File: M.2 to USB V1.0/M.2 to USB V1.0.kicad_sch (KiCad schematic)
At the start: 16 parts, among them IC1 USB2422T_MJ, IC2 TPS2041CDBVT, IC3 TPS2041CDBVT, J1 M.2 Slot, U1 APX809-46SRG-7

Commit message: updated schematic
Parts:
- added IC4: TPS61230ARNST, Component Library:RNS0007A, symbol TPS61230ARNST:TPS61230ARNST
- added R4: 100kΩ, Resistor_SMD:R_0402_1005Metric_Pad0.72x0.64mm_HandSolder, symbol Device:R_US
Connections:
- net GND: now also R4.2
- net at IC1.17 (SUSP_IND/LOCAL_PWR/(NON_REM0)): now also R4.1
- no-connect marks 58 -> 60
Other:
- moved on the sheet: C5, C6, C7, C8, IC1, R1

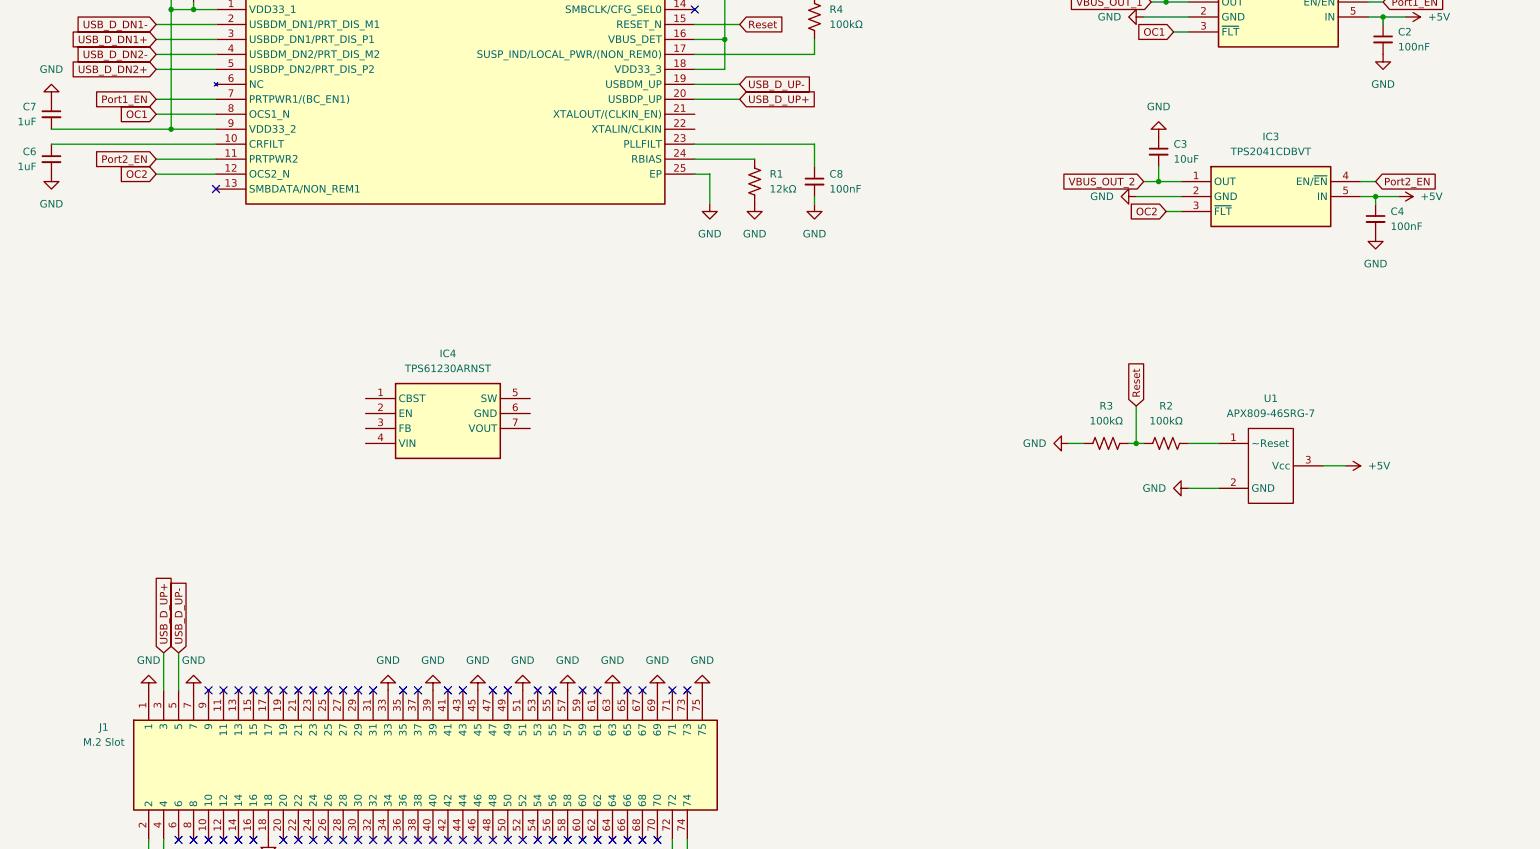
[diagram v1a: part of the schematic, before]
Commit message: finished schematic
finished schematic values of crystal caps not set. will be set after board design
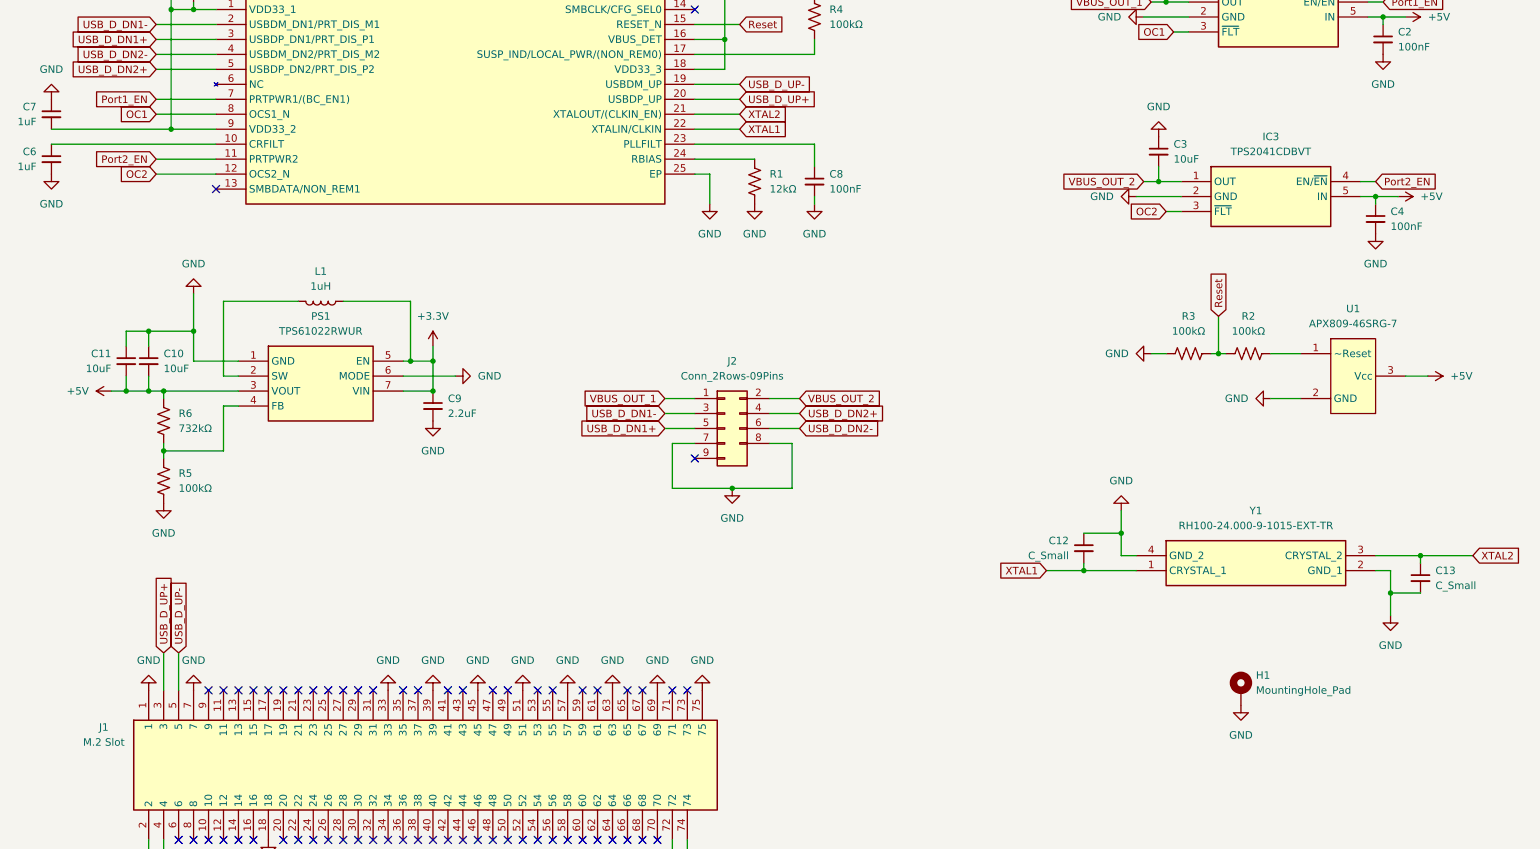
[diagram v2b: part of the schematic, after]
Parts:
- removed IC4: TPS61230ARNST, Component Library:RNS0007A, symbol TPS61230ARNST:TPS61230ARNST
- added C10, C11: 10uF, Capacitor_SMD:C_0402_1005Metric_Pad0.74x0.62mm_HandSolder, symbol Device:C_Small
- added C12, C13: C_Small, Capacitor_SMD:C_0402_1005Metric_Pad0.74x0.62mm_HandSolder, symbol Device:C_Small
- added C9: 2.2uF, Capacitor_SMD:C_0402_1005Metric_Pad0.74x0.62mm_HandSolder, symbol Device:C_Small
- added H1: MountingHole_Pad, Component Library:m.2 edge mount hole, symbol Mechanical:MountingHole_Pad
- added J2: Conn_2Rows-09Pins, symbol Connector_Generic:Conn_2Rows-09Pins
- added L1: 1uH, Inductor_SMD:L_Bourns_SRN6045TA, symbol Device:L
- added PS1: TPS61022RWUR, Component Library:TPS61022RWUR, symbol TPS61022RWUR:TPS61022RWUR
- added R5: 100kΩ, Resistor_SMD:R_0402_1005Metric_Pad0.72x0.64mm_HandSolder, symbol Device:R_US
- added R6: 732kΩ, Resistor_SMD:R_0402_1005Metric_Pad0.72x0.64mm_HandSolder, symbol Device:R_US
- added Y1: RH100-24.000-9-1015-EXT-TR, Component Library:RH10010000105050TR, symbol RH100-24_000-9-1015-EXT-TR:RH100-24.000-9-1015-EXT-TR
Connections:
- net +3.3V: now also C9.1, L1.1, PS1.5 (EN), PS1.7 (VIN)
- net +5V: now also C10.2, C11.2, PS1.3 (VOUT), R6.1
- net GND: now also C10.1, C11.1, C12.1, C13.2, C9.2, H1.1, J2.7 (Pin_7), J2.8 (Pin_8), PS1.1 (GND), PS1.6 (MODE), R5.2, Y1.2 (GND_1), Y1.4 (GND_2)
- net USB_D_DN1+: now also J2.5 (Pin_5)
- net USB_D_DN1-: now also J2.3 (Pin_3)
- net USB_D_DN2+: now also J2.4 (Pin_4)
- net USB_D_DN2-: now also J2.6 (Pin_6)
- net VBUS_OUT_1: now also J2.1 (Pin_1)
- net VBUS_OUT_2: now also J2.2 (Pin_2)
- net XTAL2: now reaches IC1.21 (XTALOUT/(CLKIN_EN))
- net XTAL2: now also C13.1, Y1.3 (CRYSTAL_2)
- net XTAL1: now reaches IC1.22 (XTALIN/CLKIN)
- net XTAL1: now also C12.2, Y1.1 (CRYSTAL_1)
- new net: PS1.4 (FB), R5.1, R6.2
- new net: L1.2, PS1.2 (SW)
- no-connect marks 60 -> 61
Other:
- moved on the sheet: R2, R3

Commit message: added all footprints
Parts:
- J2: footprint (none) -> Component Library:G821EU210AAL10Y
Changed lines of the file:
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@@
 			)
 		)
-		(property "Footprint" ""
+		(property "Footprint" "Component Library:G821EU210AAL10Y"
 			(at 137.16 107.95 0)
 			(effects

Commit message: finished pcb layout
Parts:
- J2: footprint Component Library:G821EU210AAL10Y -> Component Library:USB 2.0 Front Header
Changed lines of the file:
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@@
 			)
 		)
-		(property "Footprint" "Component Library:G821EU210AAL10Y"
+		(property "Footprint" "Component Library:USB 2.0 Front Header"
 			(at 137.16 107.95 0)
 			(effects

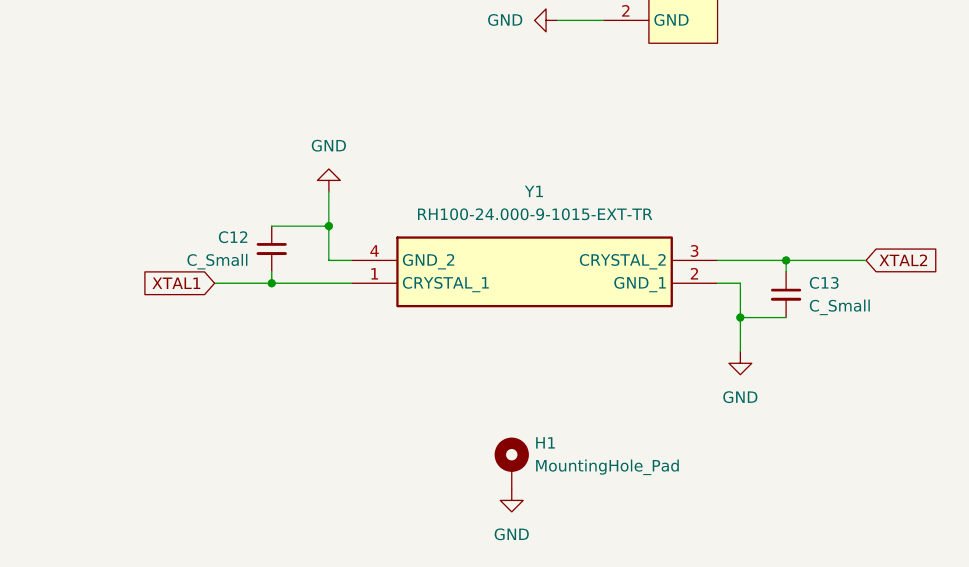
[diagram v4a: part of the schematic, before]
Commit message: updated pcb
updated pcb

calculated load caps

added 3D render
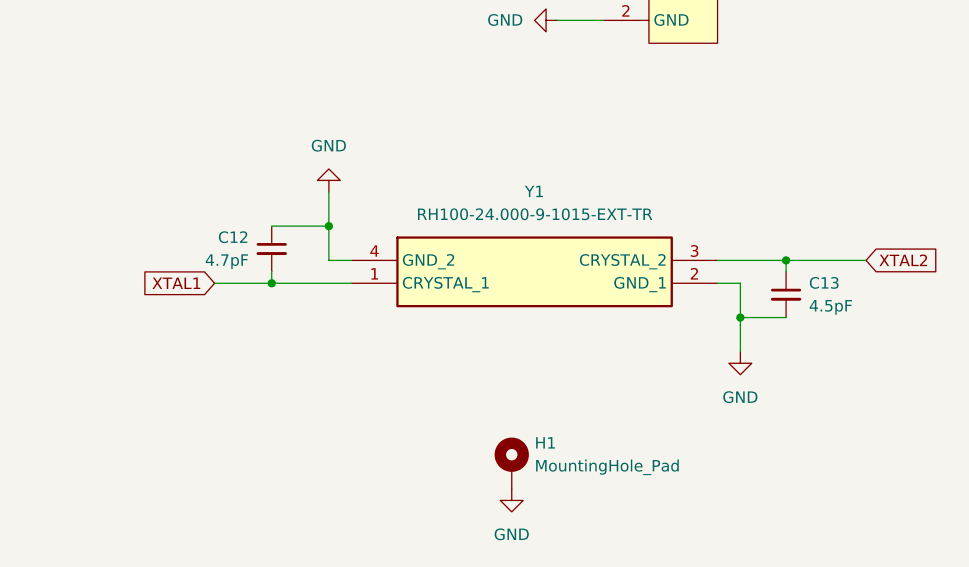
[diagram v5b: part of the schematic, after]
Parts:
- C12: value C_Small -> 4.7pF
- C13: value C_Small -> 4.5pF
- C5: footprint Capacitor_SMD:C_0402_1005Metric_Pad0.74x0.62mm_HandSolder -> Capacitor_SMD:C_0402_1005Metric
- R1: footprint Resistor_SMD:R_0402_1005Metric_Pad0.72x0.64mm_HandSolder -> Resistor_SMD:R_0402_1005Metric
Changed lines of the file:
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@@
 			)
 		)
-		(property "Footprint" "Resistor_SMD:R_0402_1005Metric_Pad0.72x0.64mm_HandSolder"
+		(property "Footprint" "Resistor_SMD:R_0402_1005Metric"
 			(at 143.256 66.294 90)
 			(effects
@@
 			)
 		)
-		(property "Value" "C_Small"
+		(property "Value" "4.7pF"
 			(at 195.58 129.5462 0)
 			(effects
@@
 			)
 		)
-		(property "Value" "C_Small"
+		(property "Value" "4.5pF"
 			(at 257.81 134.6262 0)
 			(effects
@@
 			)
 		)
-		(property "Footprint" "Capacitor_SMD:C_0402_1005Metric_Pad0.74x0.62mm_HandSolder"
+		(property "Footprint" "Capacitor_SMD:C_0402_1005Metric"
 			(at 46.99 33.02 0)
 			(effects

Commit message: Organized Schematic
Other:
- note added: "24MHz Crystal for USB Hub"
- note added: "3.3V to 5V Boost Converter"
- note added: "A+E Key Card Edge"
- note added: "Front Panel USB 2.0 Header"
- note added: "M.2 Mounting Hole"
- note added: "Reset Signal Generator"
- note added: "USB 2.0 Hub"
- note added: "USB Port Current Monitors"
- moved on the sheet: C1, C10, C11, C12, C13, C2, C3, C4, C5, C6, C7, C8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
